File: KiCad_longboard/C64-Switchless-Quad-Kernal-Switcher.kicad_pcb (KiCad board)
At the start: 2 copper layers, 21.6 x 46.4 mm, 9 parts, among them J1 Pinlist_12pin, J2 Pinlist_12pin, J3 27C256_28PDIP, J4 Wireconnections, U1 ATtiny45/85-20PU

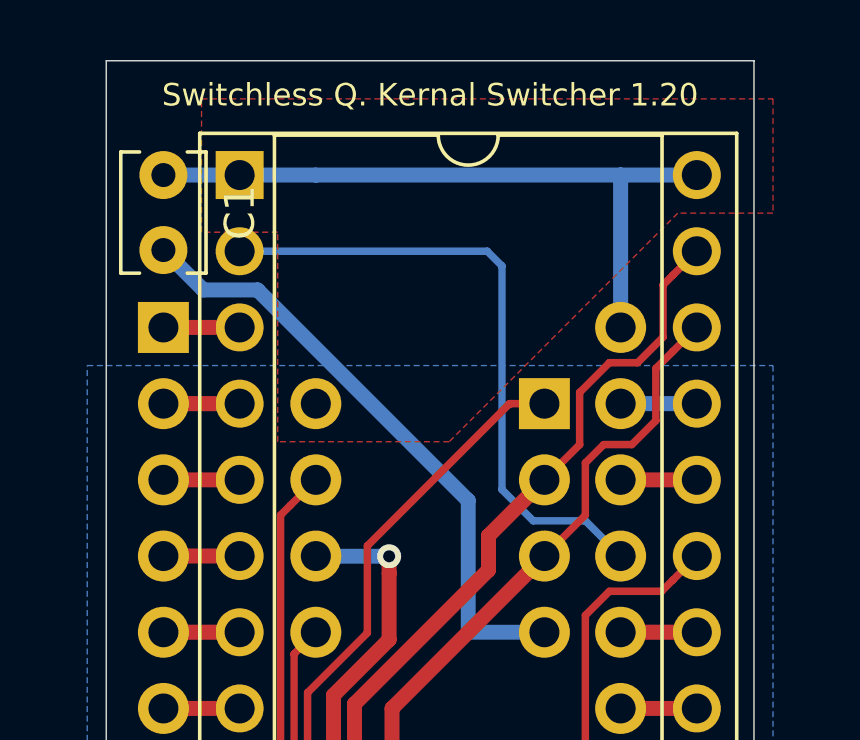
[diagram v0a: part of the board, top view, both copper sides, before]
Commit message: longboard pcb version, 8 bank support
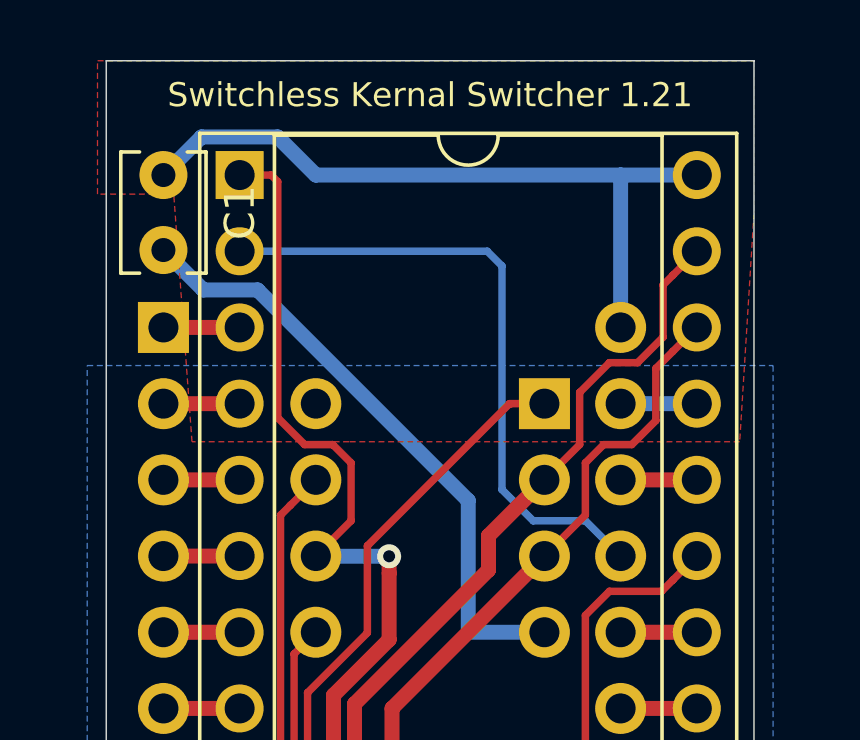
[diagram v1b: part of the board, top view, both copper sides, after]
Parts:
- C1: value C -> 100nF
- J3: value 27C256_28PDIP -> 27C256/512_28PDIP
- U1: value ATtiny45/85-20PU -> ATtiny85-20PU
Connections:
- J3 pad 1: VCC -> /A15
- R3 pad 2: /RED_LED -> /A15
- U1 pad 6: /RED_LED -> /A15
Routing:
- net /A15: track 0.00 -> 35.9 mm, vias 0 -> 1
- net /RED_LED: track 20.0 -> 0.00 mm, vias 1 -> 0
- net VCC: track 22.9 -> 23.9 mm
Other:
- board text added: "Switchless Kernal Switcher 1.21"
- board text removed: "Switchless Q. Kernal Switcher 1.20"
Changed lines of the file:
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@@
     (thickness 1.6)
     (drawings 19)
-    (tracks 124)
+    (tracks 133)
     (zones 0)
     (modules 9)
@@
   (title_block
     (title "C64 Switchless Quad Kernal Switcher (SKS64)")
-    (date 2019-07-13)
-    (rev 1.20)
+    (date 2019-07-23)
+    (rev 1.21)
     (company Bwack)
   )
@@
   (net 31 /GREEN)
   (net 32 /BLUE)
-  (net 33 /RED_LED)
+  (net 33 /A15)
   (net_class Default "This is the default net class."
     (clearance 0.2)
@@
     (add_net /A13)
     (add_net /A14)
+    (add_net /A15)
     (add_net /BLUE)
     (add_net /GREEN)
     (add_net /RED)
-    (add_net /RED_LED)
     (add_net /~EXROM~)
     (add_net /~INTRST~)
@@
       (effects (font (size 1 1) (thickness 0.15)) (justify mirror))
     )
-    (fp_text value ATtiny45/85-20PU (at 3.81 -9.95) (layer B.Fab)
+    (fp_text value ATtiny85-20PU (at 3.81 -9.95) (layer B.Fab)
       (effects (font (size 1 1) (thickness 0.15)) (justify mirror))
     )
@@
       (net 25 /A13))
     (pad 6 thru_hole oval (at 7.62 -5.08 180) (size 1.7 1.7) (drill 1) (layers *.Cu *.Mask)
-      (net 33 /RED_LED))
+      (net 33 /A15))
     (pad 2 thru_hole oval (at 0 -2.54 180) (size 1.7 1.7) (drill 1) (layers *.Cu *.Mask)
       (net 26 /A14))
@@
       (effects (font (size 1 1) (thickness 0.15)))
     )
-    (fp_text value 27C256_28PDIP (at 6.477 33.02) (layer F.Fab)
+    (fp_text value 27C256/512_28PDIP (at 6.477 33.02) (layer F.Fab)
       (effects (font (size 1 1) (thickness 0.15)))
     )
@@
     )
     (pad 1 thru_hole rect (at 0 0) (size 1.6 1.6) (drill 1) (layers *.Cu *.Mask)
-      (net 1 VCC))
+      (net 33 /A15))
     (pad 15 thru_hole oval (at 15.24 33.02) (size 1.6 1.6) (drill 1) (layers *.Cu *.Mask)
       (net 24 "Net-(J2-Pad1)"))
@@
       (effects (font (size 1 1) (thickness 0.15)))
     )
-    (fp_text value C (at 1.25 2.55 90) (layer F.Fab)
+    (fp_text value 100nF (at 1.25 2.55 90) (layer F.Fab)
       (effects (font (size 1 1) (thickness 0.15)))
     )
@@
       (net 30 /RED))
     (pad 2 thru_hole oval (at 10.16 0 90) (size 1.6 1.6) (drill 0.8) (layers *.Cu *.Mask)
-      (net 33 /RED_LED))
+      (net 33 /A15))
     (model ${KISYS3DMOD}/Resistor_THT.3dshapes/R_Axial_DIN0207_L6.3mm_D2.5mm_P10.16mm_Horizontal.wrl
       (at (xyz 0 0 0))
@@
     (effects (font (size 1 1) (thickness 0.15)) (justify mirror))
   )
-  (gr_text "Switchless Q. Kernal Switcher 1.20" (at 113.03 55.753) (layer F.SilkS)
-    (effects (font (size 0.75 0.75) (thickness 0.15)))
+  (gr_text "Switchless Kernal Switcher 1.21" (at 113.03 55.753) (layer F.SilkS)
+    (effects (font (size 0.8 0.8) (thickness 0.15)))
   )
   (gr_line (start 123.825 54.61) (end 123.825 100.965) (layer Edge.Cuts) (width 0.05))
@@
   (gr_line (start 102.235 54.61) (end 102.235 100.965) (layer Edge.Cuts) (width 0.05))
   (gr_line (start 102.235 54.61) (end 123.825 54.61) (layer Edge.Cuts) (width 0.05))
-  (segment (start 104.14 58.42) (end 106.68 58.42) (width 0.5) (layer B.Cu) (net 1))
-  (segment (start 106.68 58.42) (end 109.22 58.42) (width 0.5) (layer B.Cu) (net 1))
   (segment (start 119.38 63.5) (end 119.38 58.42) (width 0.5) (layer B.Cu) (net 1))
   (segment (start 109.22 58.42) (end 119.38 58.42) (width 0.5) (layer B.Cu) (net 1))
   (segment (start 119.38 58.42) (end 121.92 58.42) (width 0.5) (layer B.Cu) (net 1))
+  (segment (start 104.14 58.42) (end 105.41 57.15) (width 0.5) (layer B.Cu) (net 1))
+  (segment (start 107.95 57.15) (end 109.22 58.42) (width 0.5) (layer B.Cu) (net 1))
+  (segment (start 105.41 57.15) (end 107.95 57.15) (width 0.5) (layer B.Cu) (net 1))
   (segment (start 104.14 91.44) (end 106.68 91.44) (width 0.5) (layer F.Cu) (net 2))
   (segment (start 114.3 94.615) (end 114.3 96.52) (width 0.5) (layer B.Cu) (net 2))
@@
   (segment (start 111.66348 73.907652) (end 111.66348 71.693305) (width 0.5) (layer F.Cu) (net 33))
   (segment (start 116.84 78.74) (end 114.85626 80.72374) (width 0.5) (layer F.Cu) (net 33))
+  (segment (start 107.73 58.42) (end 106.68 58.42) (width 0.25) (layer F.Cu) (net 33))
+  (segment (start 107.95 58.64) (end 107.73 58.42) (width 0.25) (layer F.Cu) (net 33))
+  (segment (start 108.845997 67.404999) (end 107.95 66.509002) (width 0.25) (layer F.Cu) (net 33))
+  (segment (start 109.784001 67.404999) (end 108.845997 67.404999) (width 0.25) (layer F.Cu) (net 33))
+  (segment (start 110.395001 69.944999) (end 110.395001 68.015999) (width 0.25) (layer F.Cu) (net 33))
+  (segment (start 107.95 66.509002) (end 107.95 58.64) (width 0.25) (layer F.Cu) (net 33))
+  (segment (start 110.395001 68.015999) (end 109.784001 67.404999) (width 0.25) (layer F.Cu) (net 33))
+  (segment (start 109.22 71.12) (end 110.395001 69.944999) (width 0.25) (layer F.Cu) (net 33))
   (zone (net 2) (net_name GND) (layer B.Cu) (hatch edge 0.508)
     (connect_pads (clearance 0.508))
     (min_thickness 0.254)
-    (fill yes (arc_segments 32) (thermal_gap 1) (thermal_bridge_width 0.508))
+    (fill yes (arc_segments 32) (thermal_gap 0.7) (thermal_bridge_width 0.508))
     (polygon
       (pts
@@
     (connect_pads (clearance 0.508))
     (min_thickness 0.254)
-    (fill yes (arc_segments 32) (thermal_gap 1) (thermal_bridge_width 0.508))
+    (fill yes (arc_segments 32) (thermal_gap 0.7) (thermal_bridge_width 0.5))
     (polygon
       (pts
-        (xy 105.41 55.88) (xy 124.46 55.88) (xy 124.46 59.69) (xy 121.285 59.69) (xy 113.665 67.31)
-        (xy 107.95 67.31) (xy 107.95 60.325) (xy 105.41 60.325)
+        (xy 101.943336 54.61) (xy 123.825 54.61) (xy 123.825 59.69) (xy 123.34875 67.31) (xy 110.33125 67.31)
+        (xy 105.0925 67.31) (xy 104.483336 59.055) (xy 101.943336 59.055)
       )
     )
